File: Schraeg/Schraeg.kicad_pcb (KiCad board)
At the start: 2 copper layers, 84.5 x 128.5 mm, 116 parts, among them U1 TL074, U2 TL074, U3 V2164, U4 TL074, U5 TL074

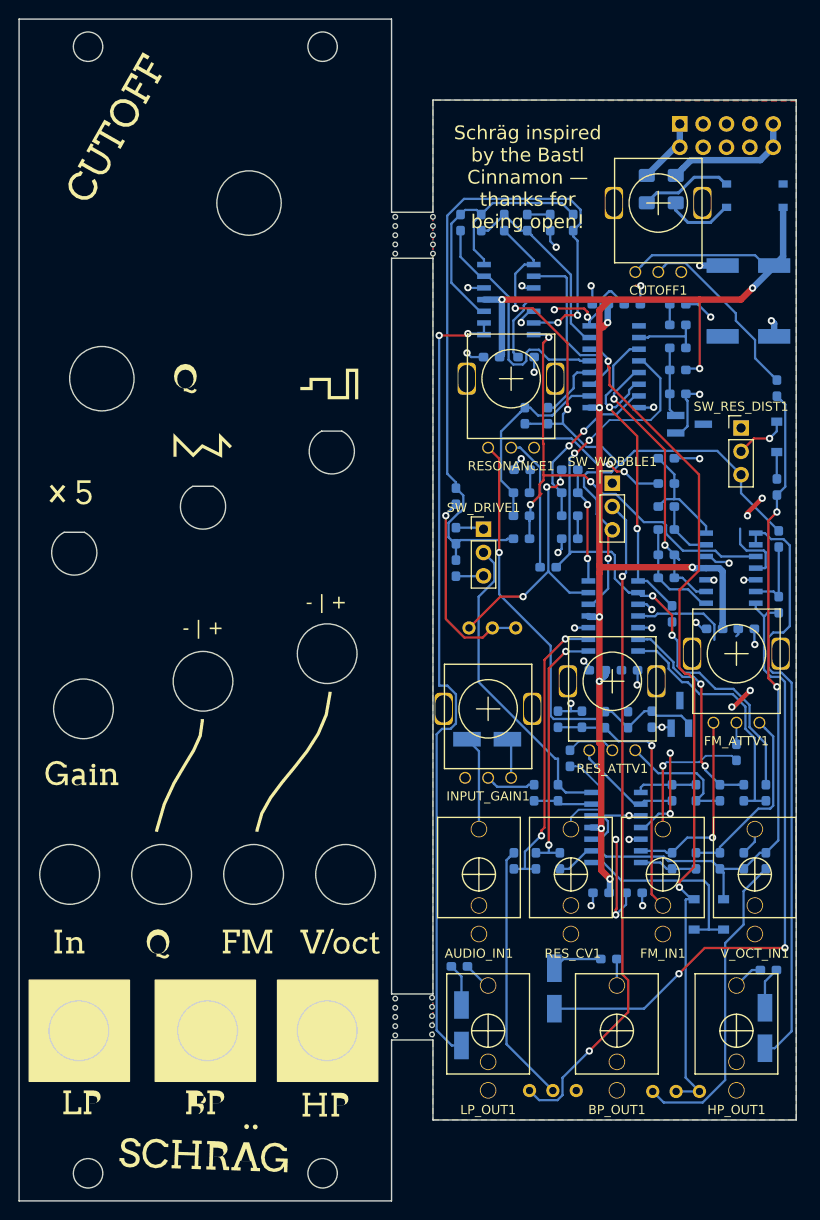
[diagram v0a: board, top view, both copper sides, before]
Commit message: Corrected alignment between panel and pcb, changed to slide switches, trimpot for resonance (leaves more space for cutoff) and new panel design.
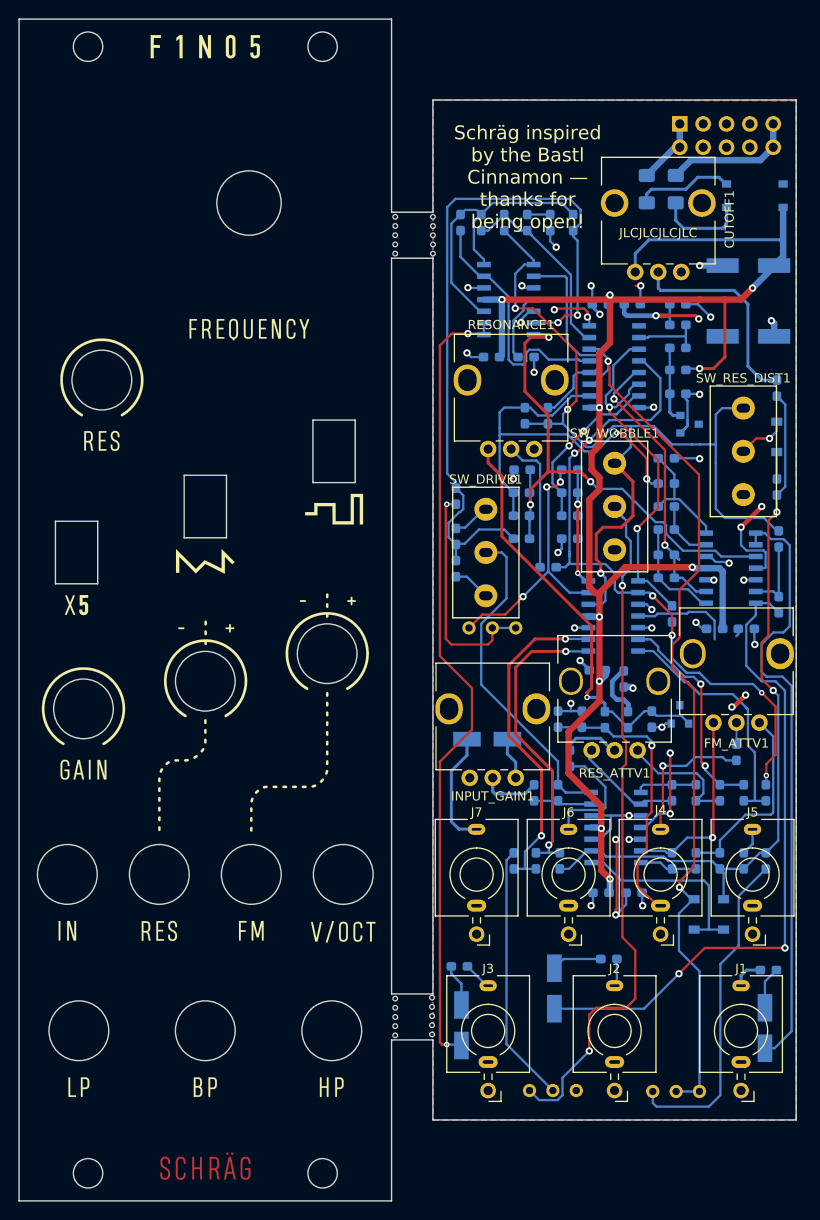
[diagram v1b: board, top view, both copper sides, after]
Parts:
- removed AUDIO_IN1, BP_OUT1, FM_IN1, HP_OUT1, LP_OUT1, RES_CV1, V_OCT_IN1: PJ301M-12, Eurocad:PJ301M-12
- removed svg2mod: G***, Schraeg:Schraeg Panel Graphics Inkscape
- added G***: LOGO, Schraeg:copper, F.Cu at (20.2, 64.2)
- added G***: LOGO, Schraeg:maskF, F.Cu at (20.2, 64.2)
- added G***: LOGO, Schraeg:silkF, F.Cu at (20.2, 64.2)
- added J1: PJ398SM, barullo_eurorack:Jack_3.5mm_QingPu_WQP-PJ398SM_Vertical_CircularHoles, F.Cu at (78.5, 116.5)
- added J2: PJ398SM, barullo_eurorack:Jack_3.5mm_QingPu_WQP-PJ398SM_Vertical_CircularHoles, F.Cu at (64.8, 116.5)
- added J3: PJ398SM, barullo_eurorack:Jack_3.5mm_QingPu_WQP-PJ398SM_Vertical_CircularHoles, F.Cu at (51.0, 116.5)
- added J4: PJ398SM, barullo_eurorack:Jack_3.5mm_QingPu_WQP-PJ398SM_Vertical_CircularHoles, F.Cu at (69.8, 99.5)
- added J5: PJ398SM, barullo_eurorack:Jack_3.5mm_QingPu_WQP-PJ398SM_Vertical_CircularHoles, F.Cu at (79.8, 99.5)
- added J6: PJ398SM, barullo_eurorack:Jack_3.5mm_QingPu_WQP-PJ398SM_Vertical_CircularHoles, F.Cu at (59.8, 99.5)
- added J7: PJ398SM, barullo_eurorack:Jack_3.5mm_QingPu_WQP-PJ398SM_Vertical_CircularHoles, F.Cu at (49.8, 99.5)
- CUTOFF1: footprint Eurocad:Alpha9mmPot -> barullo_eurorack:Potentiometer_Alps-Alpha-Bourns_Single_Vertical
- D4, D6: footprint Package_TO_SOT_SMD:SOT-23_Handsoldering -> Package_TO_SOT_SMD:SOT-23
- FM_ATTV1, INPUT_GAIN1, RESONANCE1, RES_ATTV1: footprint Eurocad:Alpha9mmPot -> barullo_eurorack:Potentiometer_Trimmer_9mm_Vertical
- SW_DRIVE1, SW_RES_DIST1, SW_WOBBLE1: footprint Connector_PinHeader_2.54mm:PinHeader_1x03_P2.54mm_Vertical -> barullo_eurorack:SW_NKK_CS1xA
- moved INPUT_GAIN1 8.08 mm to (54.0, 82.5), turned to 90 degrees
- moved RESONANCE1 8.05 mm to (56.0, 46.8), turned to 90 degrees
- moved RES_ATTV1 7.99 mm to (67.2, 79.5), turned to 90 degrees
- moved CUTOFF1 7.91 mm to (72.0, 27.5), turned to 90 degrees
- moved FM_ATTV1 7.91 mm to (80.5, 76.5), turned to 90 degrees
- moved R22 3.58 mm to (47.5, 59.8), turned to 270 degrees
- moved R21 3.45 mm to (47.5, 56.2), turned to 90 degrees
- moved SW_DRIVE1 2.55 mm to (50.8, 58.0)
- moved SW_RES_DIST1 2.55 mm to (78.8, 47.0)
- moved SW_WOBBLE1 2.55 mm to (64.8, 53.0)
- moved C21 1.14 mm to (65.8, 71.8), turned to 270 degrees
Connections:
- CUTOFF1 pad 1: -12V -> GND
- CUTOFF1 pad 3: GND -> -12V
- INPUT_GAIN1 pad 1: GND -> Net-(C2-Pad2)
- INPUT_GAIN1 pad 3: Net-(C2-Pad2) -> GND
- R2 pad 2: Net-(FM_ATTV1-Pad1) -> Net-(FM_ATTV1-Pad3)
- R5 pad 1: Net-(FM_ATTV1-Pad3) -> Net-(FM_ATTV1-Pad1)
- R8 pad 2: Net-(FM_ATTV1-Pad3) -> Net-(FM_ATTV1-Pad1)
- RESONANCE1 pad 1: 5V_REF -> GND
- RESONANCE1 pad 3: GND -> 5V_REF
- RES_ATTV1 pad 1: Net-(R3-Pad2) -> Net-(R11-Pad2)
- RES_ATTV1 pad 3: Net-(R11-Pad2) -> Net-(R3-Pad2)
- SW_DRIVE1 pad 1: Net-(R22-Pad2) -> Net-(R21-Pad2)
- SW_DRIVE1 pad 3: Net-(R21-Pad2) -> Net-(R22-Pad2)
- SW_RES_DIST1 pad 1: (no net) -> /Filter Core/RES_MOD
- SW_RES_DIST1 pad 3: /Filter Core/RES_MOD -> Net-(SW_RES_DIST1-Pad3)
- SW_WOBBLE1 pad 1: (no net) -> /Filter Core/RES_MOD
- SW_WOBBLE1 pad 3: /Filter Core/RES_MOD -> Net-(SW_WOBBLE1-Pad3)
- U1 pad 6: Net-(FM_ATTV1-Pad1) -> Net-(FM_ATTV1-Pad3)
- U3 pad 1: (no net) -> Net-(U3-Pad1)
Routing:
- net /Filter Core/RES_MOD: track 83.3 -> 100.3 mm
- net +12V: track 65.9 -> 74.9 mm, vias 10 -> 12
- net -12V: track 165.0 -> 173.7 mm
- net Net-(R4-Pad1): track 27.7 -> 33.2 mm
- net Net-(R1-Pad1): track 31.8 -> 36.7 mm
- net Net-(C10-Pad2): track 40.7 -> 45.5 mm
- net Net-(RV_SAW_OCTAVE1-Pad1): track 72.2 -> 77.0 mm
- net 5V_REF: track 50.4 -> 46.4 mm
- net Net-(R26-Pad1): track 21.8 -> 25.1 mm
- net Net-(R28-Pad1): track 52.1 -> 54.7 mm
- net Net-(CUTOFF1-Pad2): track 20.2 -> 22.7 mm
- net Net-(C2-Pad1): track 10.3 -> 12.8 mm
- net /Filter Core/BP_OUT: track 68.9 -> 71.3 mm
- net Net-(D5-Pad1): track 7.57 -> 9.83 mm
- net /Filter Core/RES_CV: track 38.0 -> 39.9 mm
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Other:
- outline, holes or cut-outs redrawn
- board text added: "JLCJLCJLCJLC"
- board text added: "Rework by F1N05"
- board text added: "Schräg v0.2.2 Barnaby Walters waterpigs.co.uk cc-by-sa 2021"
- board text removed: "- | +"
- board text removed: "Schräg v0.2.1 Barnaby Walters waterpigs.co.uk cc-by-sa 2021"

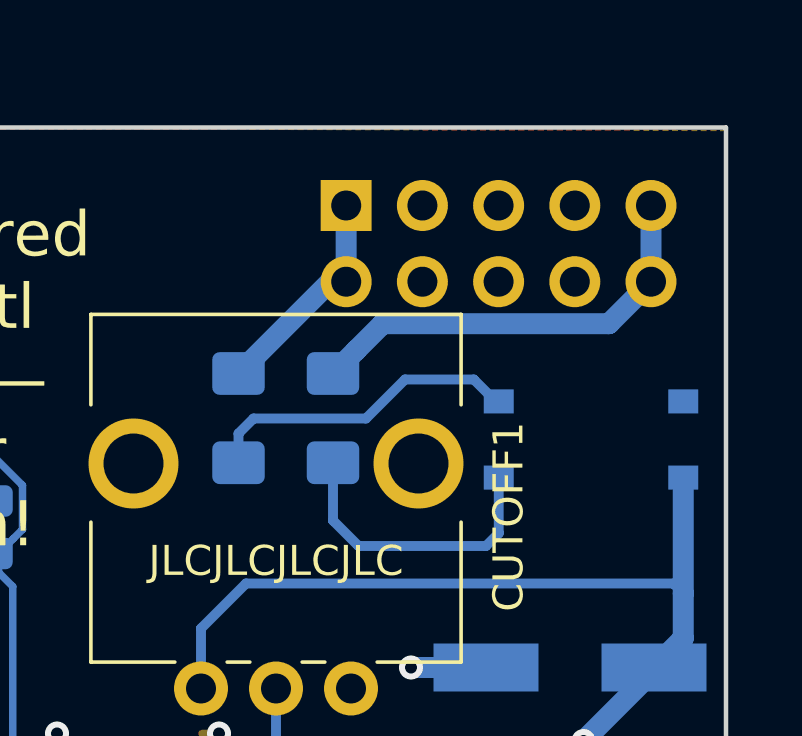
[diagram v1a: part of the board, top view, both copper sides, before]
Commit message: Changed power symbol to generic connector
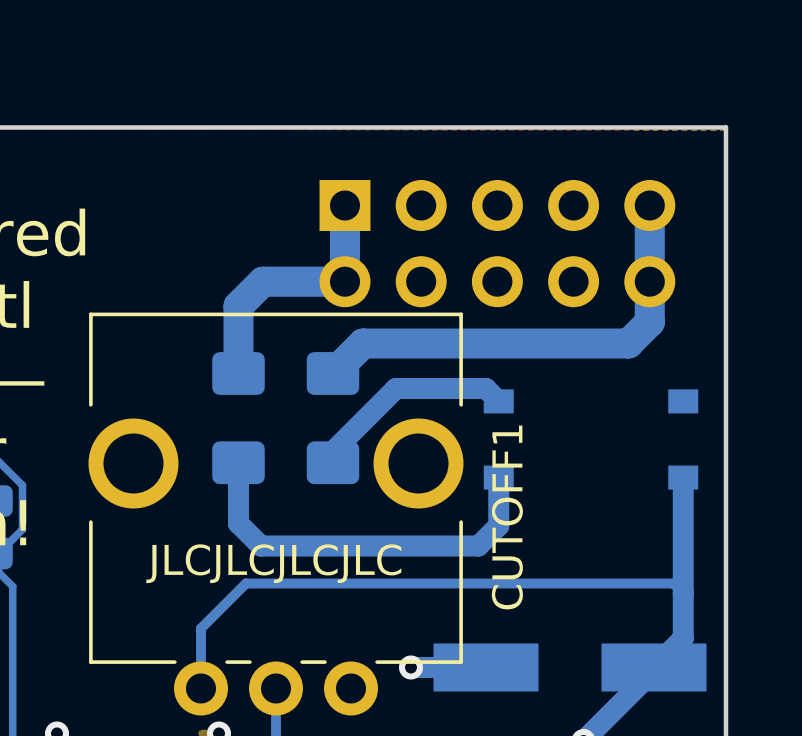
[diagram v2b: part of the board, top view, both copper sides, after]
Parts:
- removed PWR_IN1: EURO_PWR_2x5, Connector_PinHeader_2.54mm:PinHeader_2x05_P2.54mm_Vertical
- added J8: POWER, Connector_PinHeader_2.54mm:PinHeader_2x05_P2.54mm_Vertical, B.Cu at (71.8, 11.4)
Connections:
- F1 pad 1: Net-(D5-Pad2) -> Net-(D5-Pad1)
- F2 pad 1: Net-(D5-Pad1) -> Net-(D5-Pad2)
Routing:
- net Net-(D5-Pad2): track 10.7 -> 6.95 mm
- net Net-(D5-Pad1): track 9.83 -> 12.9 mm
- net Net-(F1-Pad2): track 7.40 -> 8.68 mm
- net Net-(F2-Pad2): track 14.4 -> 15.2 mm

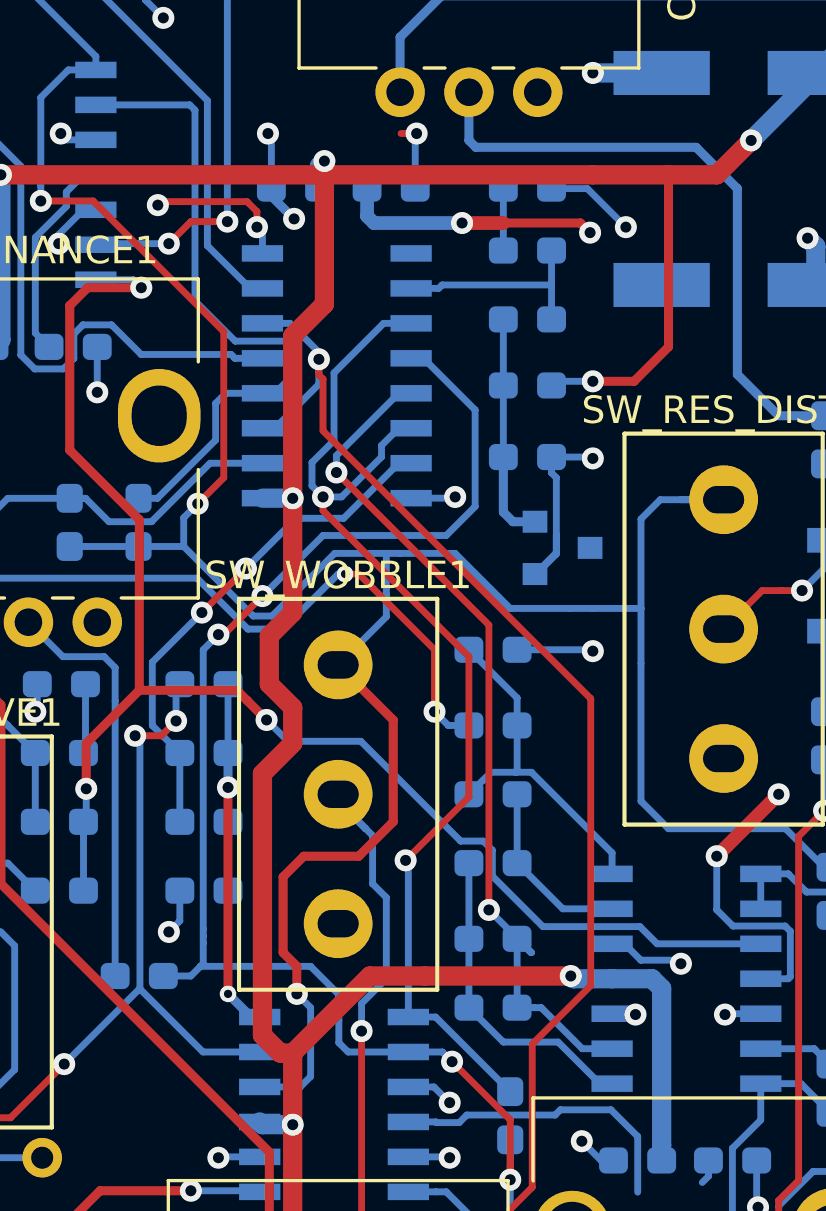
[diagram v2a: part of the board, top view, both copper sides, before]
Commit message: V2164 symbol in a new library to avoid missing dependencies.
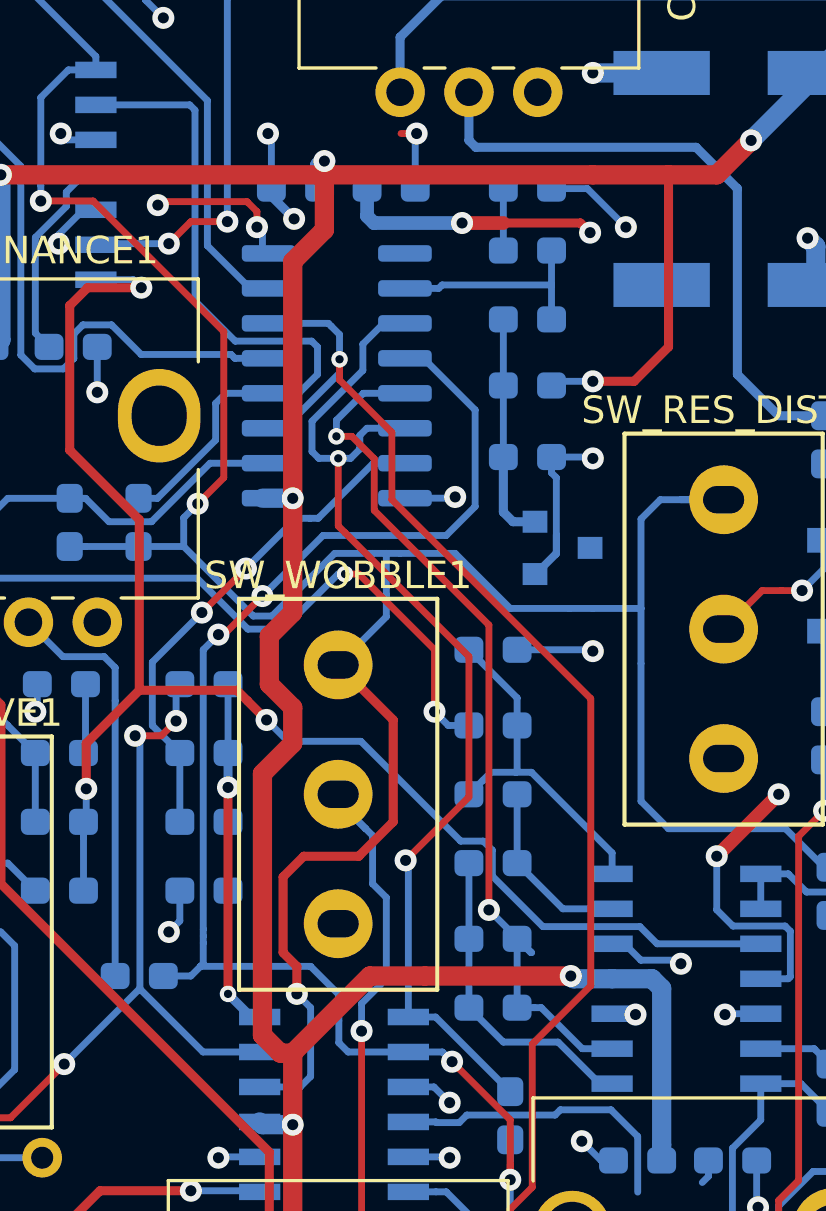
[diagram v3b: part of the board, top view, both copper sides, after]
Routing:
- net Net-(C11-Pad2): track 25.3 -> 26.8 mm
- net /Filter Core/FREQ_CV: track 97.7 -> 98.6 mm
- net /Filter Core/RES_CV: track 39.9 -> 39.0 mm
- net Net-(C9-Pad2): track 31.9 -> 32.8 mm
